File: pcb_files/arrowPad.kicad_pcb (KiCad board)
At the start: 2 copper layers, 101.6 x 83.8 mm, 60 parts, among them J1 AudioJack3_Ground, J2 AudioJack3_Ground, K1 KEYSW, K10 KEYSW, K11 KEYSW, K12 KEYSW, K13 KEYSW, K14 KEYSW, K15 KEYSW, K16 KEYSW, K2 KEYSW, K3 KEYSW, K4 KEYSW, K5 KEYSW, K6 KEYSW, K7 KEYSW, K8 KEYSW, K9 KEYSW, U1 ProMicro, U2 NRF24L01_Breakout, U3 ADG417BN, U4 AMS1117-3.3, U5 ADG417BN, U6 ADG417BN, U7 TLC5940PWP

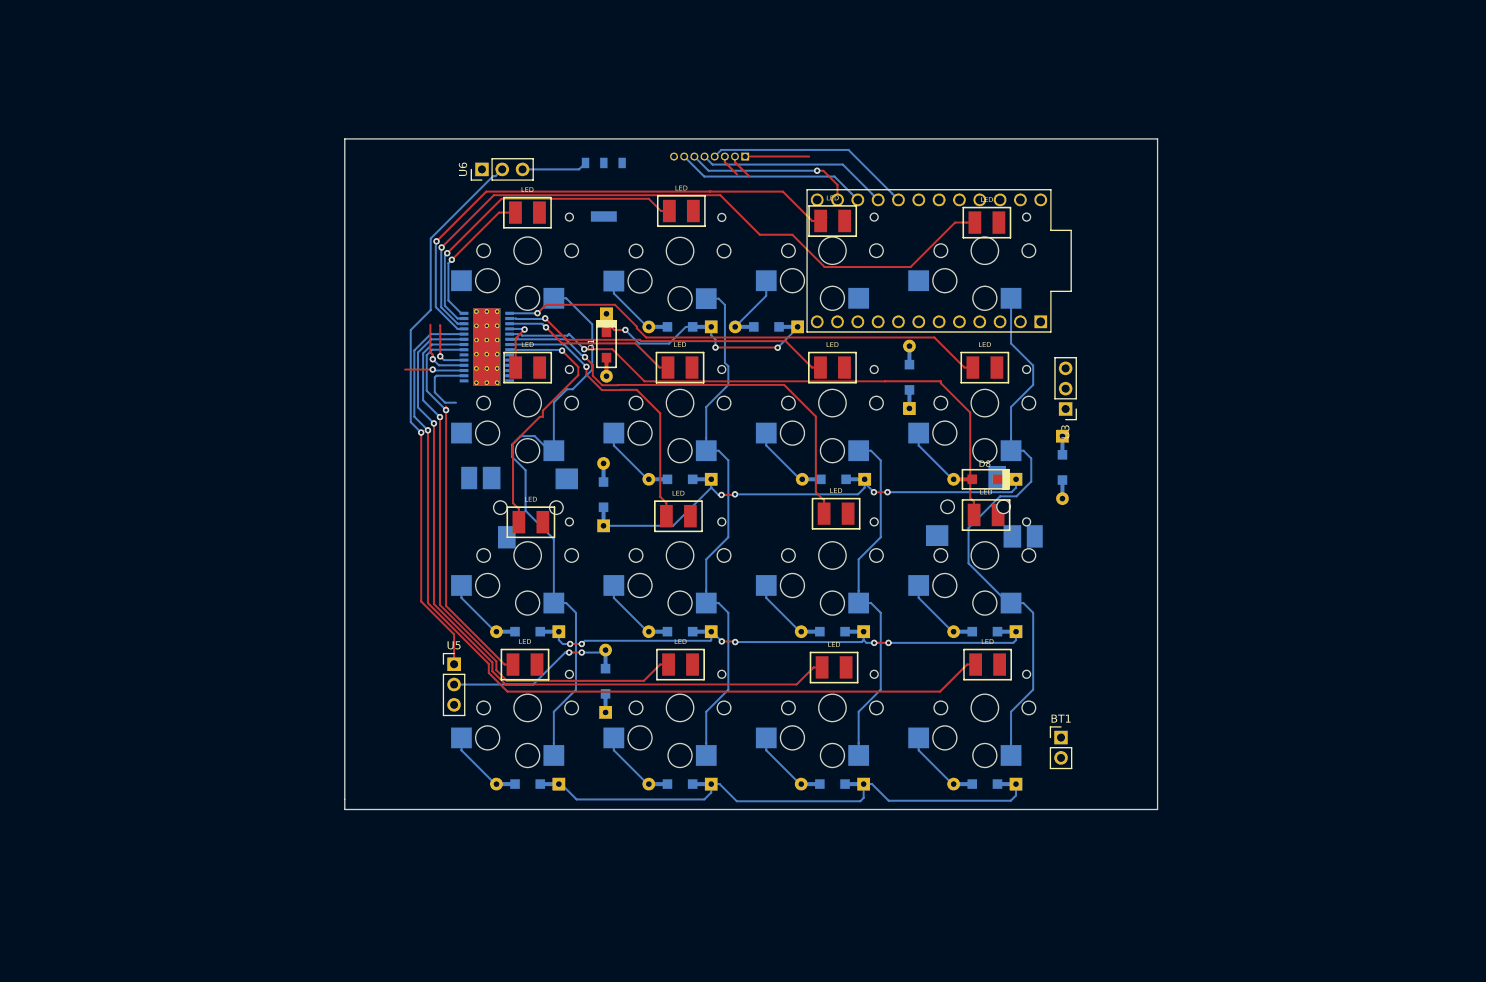
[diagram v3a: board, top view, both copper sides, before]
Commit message: matrix and nrf24l01 traces
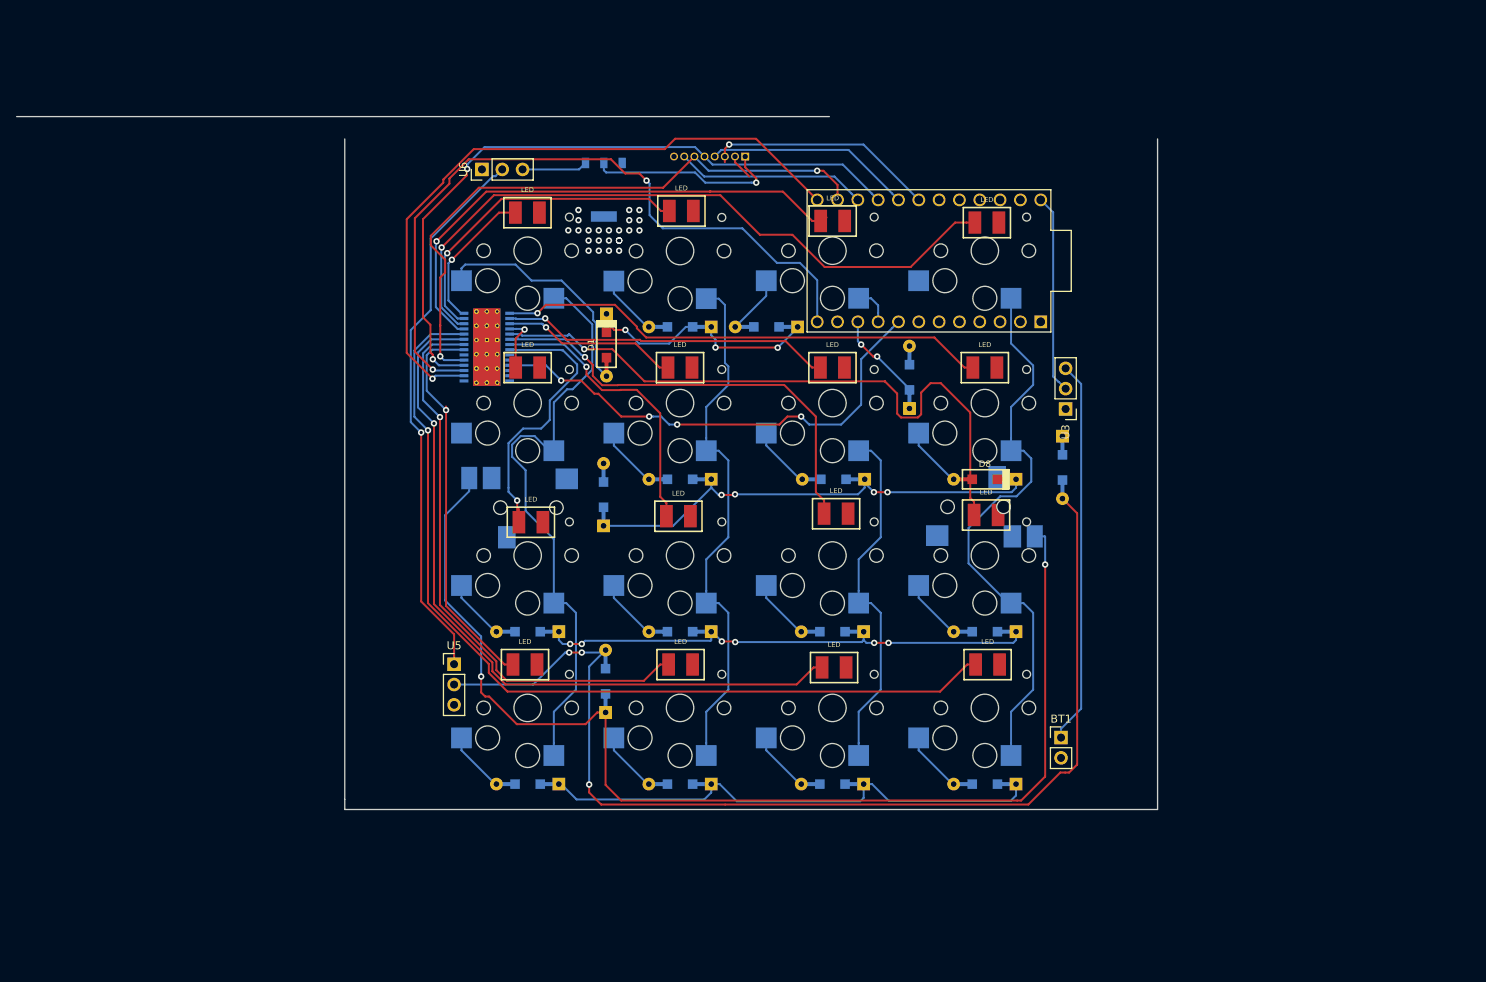
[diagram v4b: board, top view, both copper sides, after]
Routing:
- net Net-(J1-Pad1): track 0.00 -> 145.1 mm, vias 0 -> 2
- net Net-(R1-Pad2): track 20.7 -> 137.3 mm, vias 2 -> 3
- net Net-(U1-Pad12): track 7.41 -> 91.3 mm, vias 1 -> 2
- net Net-(U1-Pad13): track 8.79 -> 84.2 mm, vias 0 -> 1
- net /GSCLK: track 0.00 -> 61.1 mm, vias 0 -> 4
- net Net-(U1-Pad16): track 32.6 -> 86.4 mm, vias 1 -> 2
- net Net-(U1-Pad14): track 28.3 -> 77.6 mm
- net Net-(BT1-Pad1): track 0.00 -> 48.0 mm
- net Net-(D1-Pad2): track 0.00 -> 29.4 mm
- net Net-(U1-Pad18): track 2.88 -> 29.0 mm, vias 0 -> 1
- net /RAW1: track 0.00 -> 24.9 mm
- net Net-(U2-Pad2): track 8.00 -> 24.6 mm, vias 0 -> 1
- net /Row1: track 28.0 -> 39.5 mm, vias 3 -> 5
- net Net-(D23-Pad2): track 74.9 -> 81.4 mm
- net /Col3: track 44.5 -> 49.4 mm
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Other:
- board size 101.6 x 83.8 mm -> 142.6 x 86.6 mm

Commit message: finished traces
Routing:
- net /RAW1: track 24.9 -> 196.4 mm, vias 0 -> 3
- net Net-(J1-Pad2): track 0.00 -> 127.6 mm, vias 0 -> 3
- net /VCC1: track 70.1 -> 179.2 mm, vias 1 -> 2
- net /Row4: track 65.9 -> 165.8 mm
- net /Col1: track 75.0 -> 129.6 mm, vias 0 -> 2
- net /Row2: track 58.6 -> 111.9 mm, vias 4 -> 6
- net /Col2: track 66.7 -> 118.2 mm, vias 0 -> 2
- net /Row3: track 62.8 -> 106.5 mm, vias 6 -> 7
- net /Col3: track 49.4 -> 92.1 mm, vias 0 -> 2
- net Net-(J1-Pad1): track 145.1 -> 181.2 mm, vias 2 -> 5
- net Net-(D5-Pad2): track 0.00 -> 21.8 mm, vias 0 -> 2
- net /Row1: track 39.5 -> 55.4 mm
- net /Col4: track 71.6 -> 86.6 mm
- net Net-(D4-Pad2): track 0.00 -> 9.72 mm
- net /GSCLK: track 61.1 -> 63.9 mm
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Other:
- board size 142.6 x 86.6 mm -> 90.2 x 85.1 mm

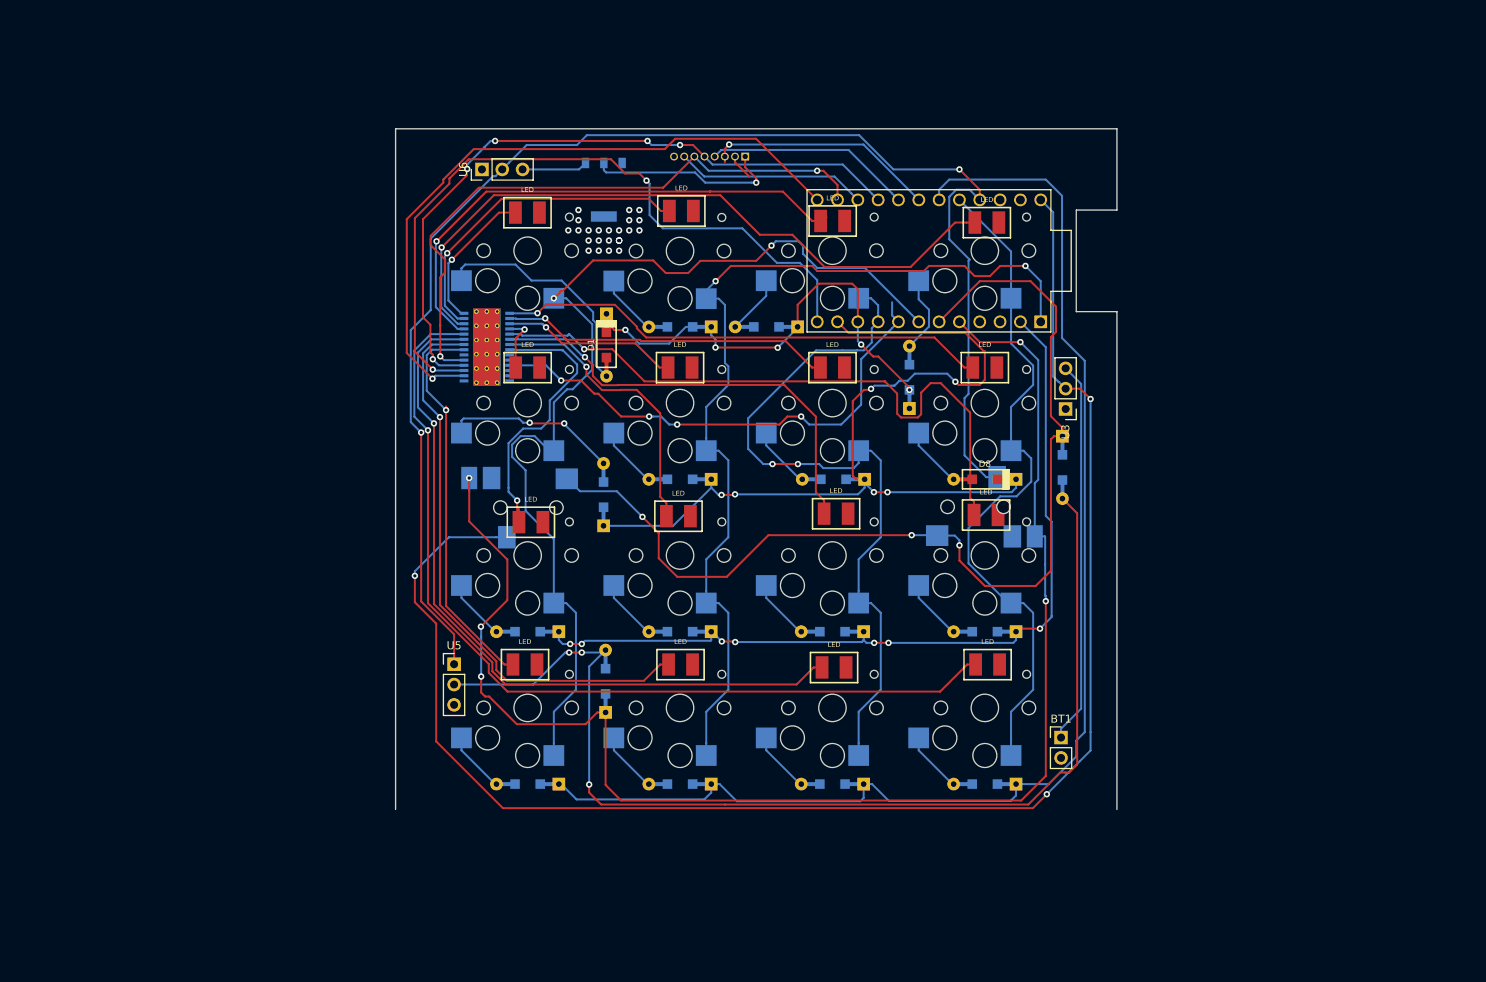
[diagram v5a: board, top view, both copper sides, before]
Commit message: adding TLC5940 connections
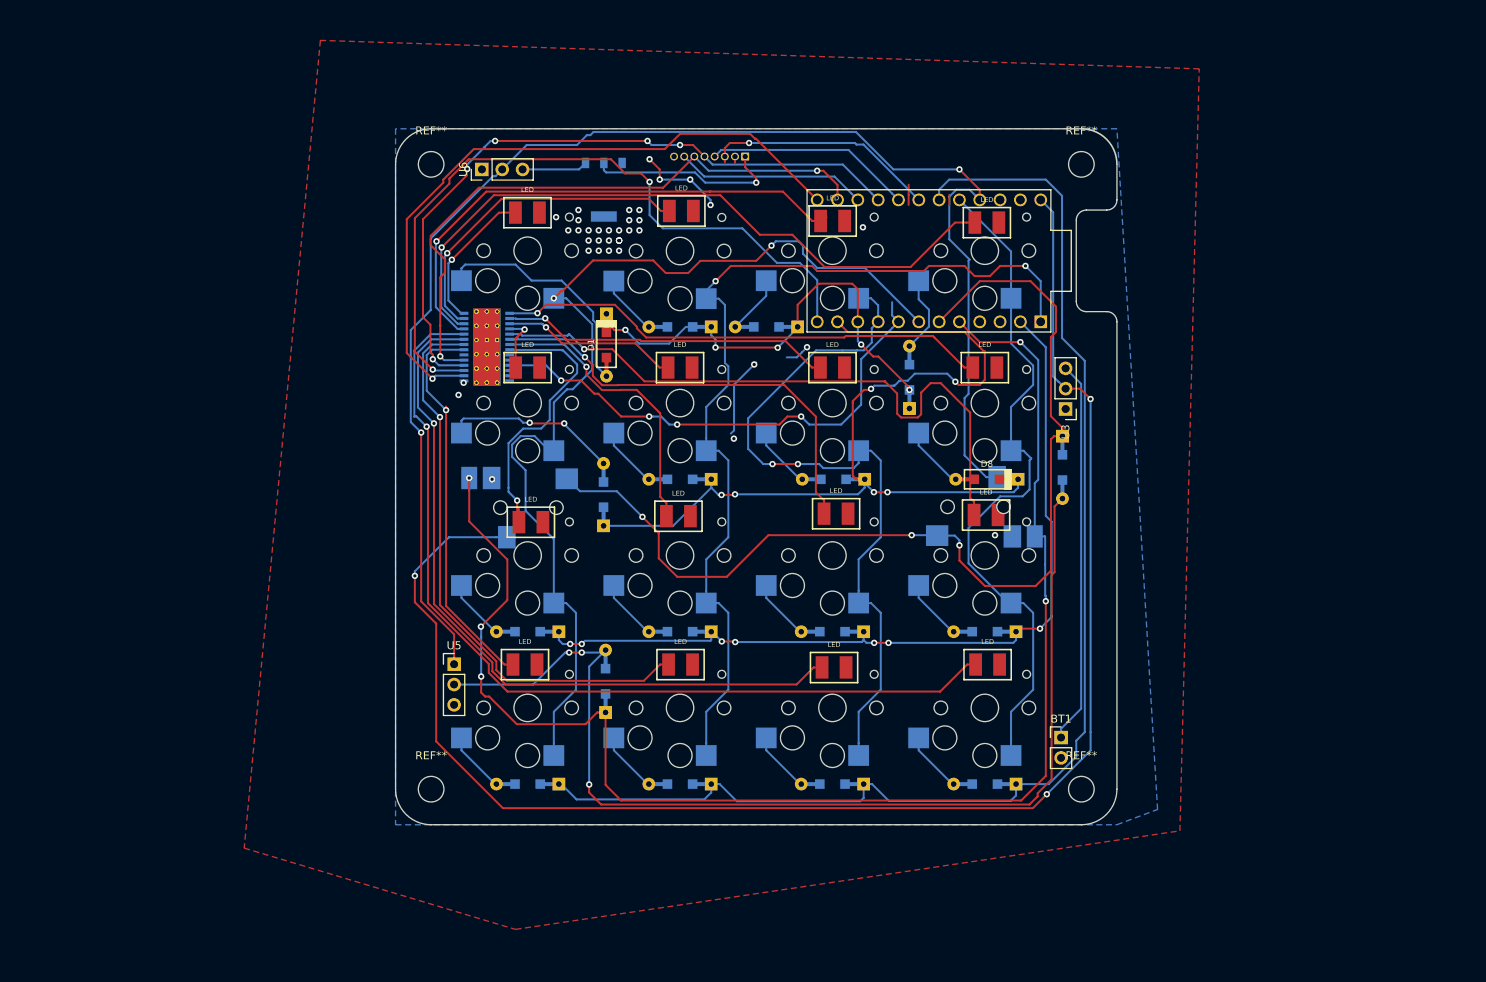
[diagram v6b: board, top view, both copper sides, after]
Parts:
- added REF**: MountingHole_3.2mm_M3, MountingHole:MountingHole_3.2mm_M3, F.Cu at (118.7, 132.1)
- added REF**: MountingHole_3.2mm_M3, MountingHole:MountingHole_3.2mm_M3, F.Cu at (200.0, 132.1)
- added REF**: MountingHole_3.2mm_M3, MountingHole:MountingHole_3.2mm_M3, F.Cu at (200.0, 54.0)
- added REF**: MountingHole_3.2mm_M3, MountingHole:MountingHole_3.2mm_M3, F.Cu at (118.7, 54.0)
- moved D8 0.25 mm to (188.2, 93.3)
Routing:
- net /GND1: track 3.97 -> 25.8 mm, vias 0 -> 13
- net (no net): track 0.00 -> 3.81 mm
- net Net-(R1-Pad2): track 137.3 -> 135.0 mm
- net Net-(U1-Pad13): track 84.2 -> 84.7 mm
- added copper zone on B.Cu, net /GND1
- added copper zone on F.Cu, net /GND1
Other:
- board size 90.2 x 85.1 mm -> 90.2 x 87 mm

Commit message: reworked led wiring
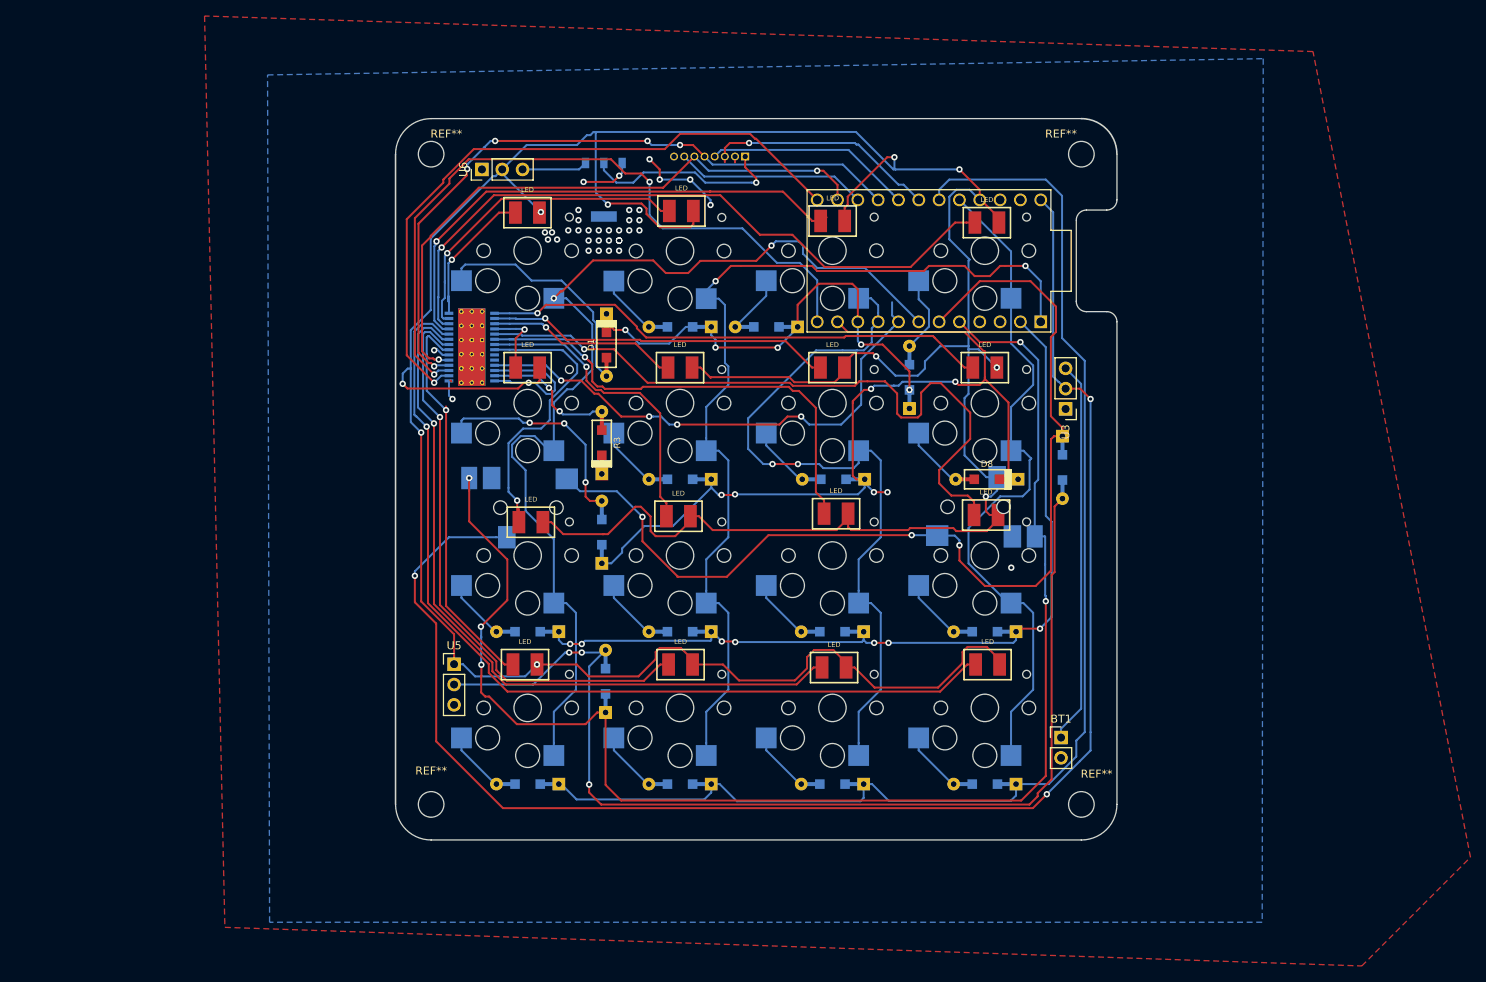
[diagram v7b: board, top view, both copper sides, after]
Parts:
- removed the REF** at (118.7, 132.1)
- removed the REF** at (200.0, 132.1)
- removed the REF** at (200.0, 54.0)
- removed the REF** at (118.7, 54.0)
- added R3: R, keyboard_parts:D_SOD123_axial, F.Cu at (140.1, 88.8)
- added REF**: MountingHole_3.2mm_M3, MountingHole:MountingHole_3.2mm_M3, F.Cu at (200.0, 52.7)
- added REF**: MountingHole_3.2mm_M3, MountingHole:MountingHole_3.2mm_M3, F.Cu at (118.7, 52.7)
- added REF**: MountingHole_3.2mm_M3, MountingHole:MountingHole_3.2mm_M3, F.Cu at (118.7, 134.0)
- added REF**: MountingHole_3.2mm_M3, MountingHole:MountingHole_3.2mm_M3, F.Cu at (200.0, 134.0)
- moved D5 4.69 mm to (140.1, 99.9)
- moved U7 1.88 mm to (123.8, 76.8)
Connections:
- D20 pad 1: /GND1 -> /VCC1
- D21 pad 1: /GND1 -> /VCC1
- D22 pad 1: /GND1 -> /VCC1
- D23 pad 1: /GND1 -> /VCC1
- D24 pad 1: /GND1 -> /VCC1
- D25 pad 1: /GND1 -> /VCC1
- D26 pad 1: /GND1 -> /VCC1
- D27 pad 1: /GND1 -> /VCC1
- D28 pad 1: /GND1 -> /VCC1
- D29 pad 1: /GND1 -> /VCC1
- D30 pad 1: /GND1 -> /VCC1
- D31 pad 1: /GND1 -> /VCC1
- D32 pad 1: /GND1 -> /VCC1
- D33 pad 1: /GND1 -> /VCC1
- D34 pad 1: /GND1 -> /VCC1
- D35 pad 1: /GND1 -> /VCC1
- U7 pad 26: Net-(U7-Pad26) -> /VCC1
- U7 pad 28: Net-(U7-Pad28) -> /VCC1
- U7 pad 6: Net-(U7-Pad6) -> /GND1
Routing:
- net /VCC1: track 179.5 -> 470.3 mm, vias 2 -> 11
- net Net-(R3-Pad2): track 0.00 -> 16.6 mm, vias 0 -> 2
- net Net-(D23-Pad2): track 81.4 -> 88.0 mm
- net Net-(D5-Pad2): track 21.8 -> 27.4 mm, vias 2 -> 3
- net (no net): track 3.81 -> 0.00 mm
- net Net-(D22-Pad2): track 56.7 -> 59.7 mm
- net Net-(D21-Pad2): track 36.2 -> 38.5 mm
- net Net-(D27-Pad2): track 62.0 -> 63.8 mm
- net Net-(D26-Pad2): track 41.5 -> 43.3 mm
- net Net-(D25-Pad2): track 22.1 -> 24.0 mm
- net Net-(D24-Pad2): track 7.14 -> 9.02 mm
- net Net-(D20-Pad2): track 36.1 -> 38.0 mm
- net /GSCLK: track 63.9 -> 65.8 mm
- net /GND1: track 25.8 -> 23.9 mm
- net /Row1: track 55.4 -> 56.9 mm
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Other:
- board size 90.2 x 87 mm -> 90.2 x 90.2 mm
